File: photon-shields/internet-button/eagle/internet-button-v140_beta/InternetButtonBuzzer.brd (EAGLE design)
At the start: 65.5 x 65.5 mm, 43 parts

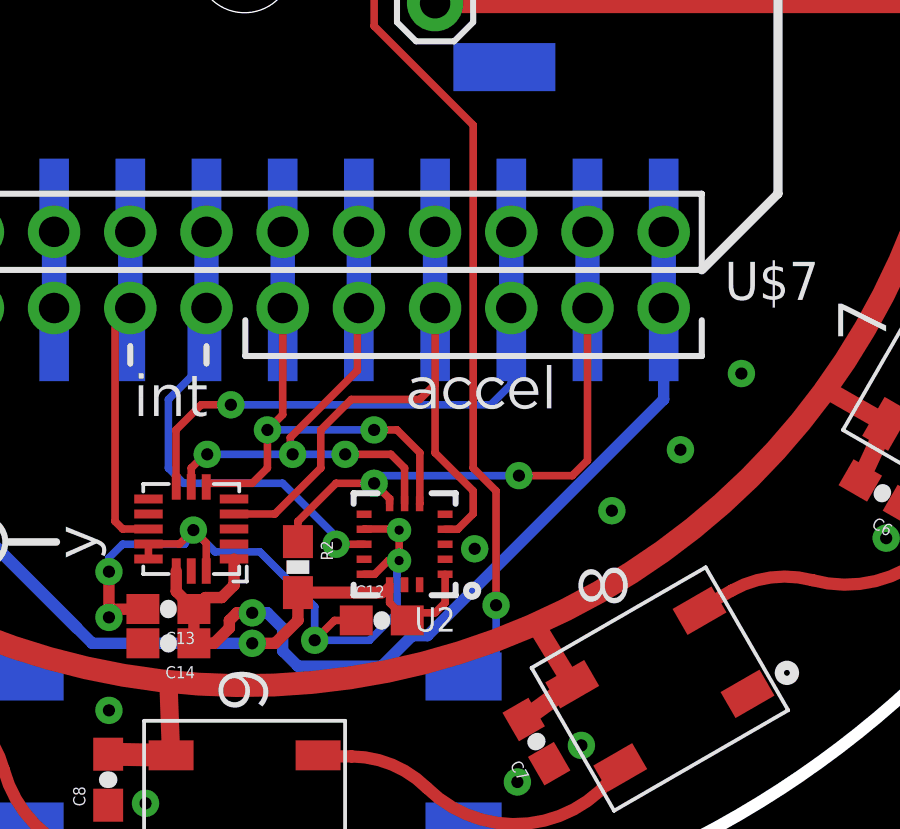
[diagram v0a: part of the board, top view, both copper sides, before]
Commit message: update the design file since i catch some error from last version
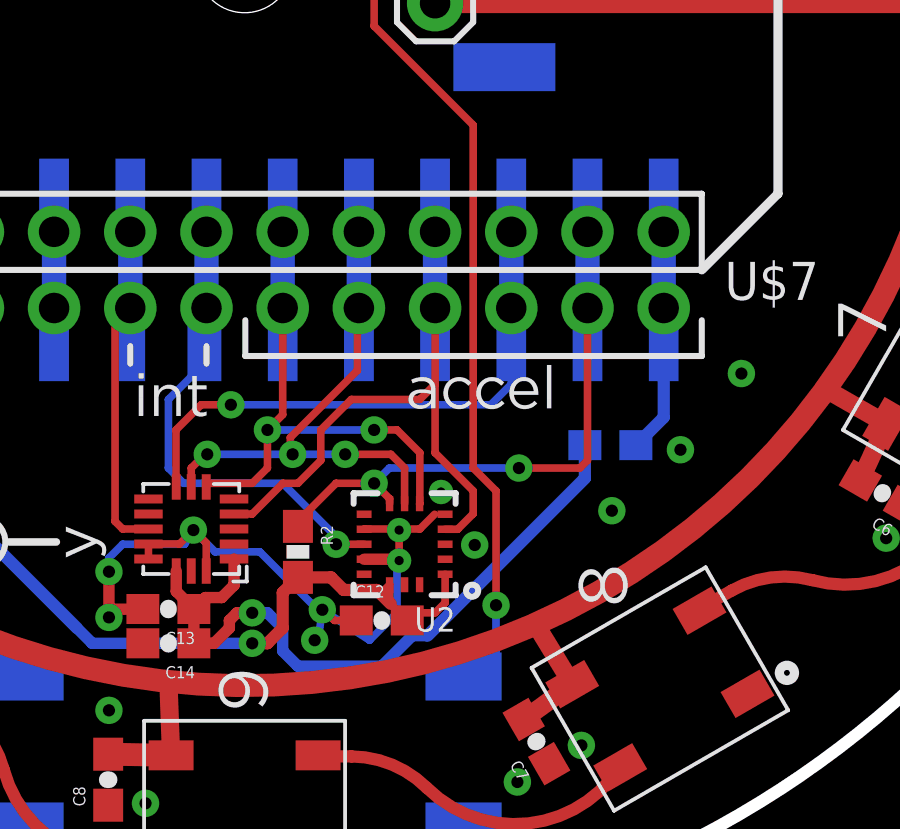
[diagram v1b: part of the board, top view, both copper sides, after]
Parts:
- added R3: 470, SparkFun-Resistors:0603-RES
- R2: value 470 -> 10K
- moved R2 0.51 mm to (36.1, 13.5)
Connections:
- removed net GND@1: U2.5
- new net N$4: R3.1, U$7.12, U$7.12B, U$7.@12, U$7.@12B
- net A0: now also R3.2; no longer U$7.12, U$7.12B, U$7.@12, U$7.@12B
- net GND: now also U2.12, U2.5; no longer U2.13
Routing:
- net A0: track 34.9 -> 23.7 mm
- net N$4: track 0.00 -> 10.5 mm
- net GND: track 73.9 -> 75.3 mm, vias 31 -> 33
- net +3V3: track 69.0 -> 70.0 mm

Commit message: update the pcb file for internet button
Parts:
- removed 12: M01PTH, SparkFun-Connectors:1X01
- removed C14: 10uF, SparkFun-Passives:0603-CAP
- removed R3: 470, SparkFun-Resistors:0603-RES
- moved 3.3V 2.93 mm to (23.2, 49.8)
- moved GND 2.54 mm to (40.6, 49.7)
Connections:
- removed net A0: C13.1, C14.1, R3.2, U1.P$1, U1.P$14
- net +3V3: now also C13.1, U1.P$1, U1.P$14
- net D6: now also U$5.3
- net GND: now also U$5.1; no longer C14.2
- net N$4: no longer R3.1
- net N$5: no longer 12.1
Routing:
- net GND: track 75.3 -> 348.5 mm, vias 33 -> 23
- net 5V: track 150.3 -> 206.1 mm, vias 0 -> 11
- net A0: track 23.7 -> 0.00 mm, vias 1 -> 0
- net N$3: track 12.0 -> 0.00 mm, vias 1 -> 0
- net +3V3: track 70.0 -> 76.9 mm
- net D7: track 46.1 -> 50.9 mm
- net D5: track 20.3 -> 24.6 mm, vias 0 -> 1
- net N$4: track 10.5 -> 7.11 mm
- net D6: track 34.0 -> 37.3 mm, vias 1 -> 2
- net D4: track 50.2 -> 48.5 mm
- net A1: track 22.6 -> 21.4 mm
- net D0: track 14.2 -> 15.4 mm
- net N$5: track 11.6 -> 10.5 mm
- removed copper zone on layer 1, net GND
- removed copper zone on layer 16, net GND
